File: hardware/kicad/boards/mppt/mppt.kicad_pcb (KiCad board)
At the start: 2 copper layers, 140 x 68 mm, 21 parts, among them J1 PV ind, J2 til lager (V3), J3 sense -> Arduino, Q1 TIP41A, U1 LM358

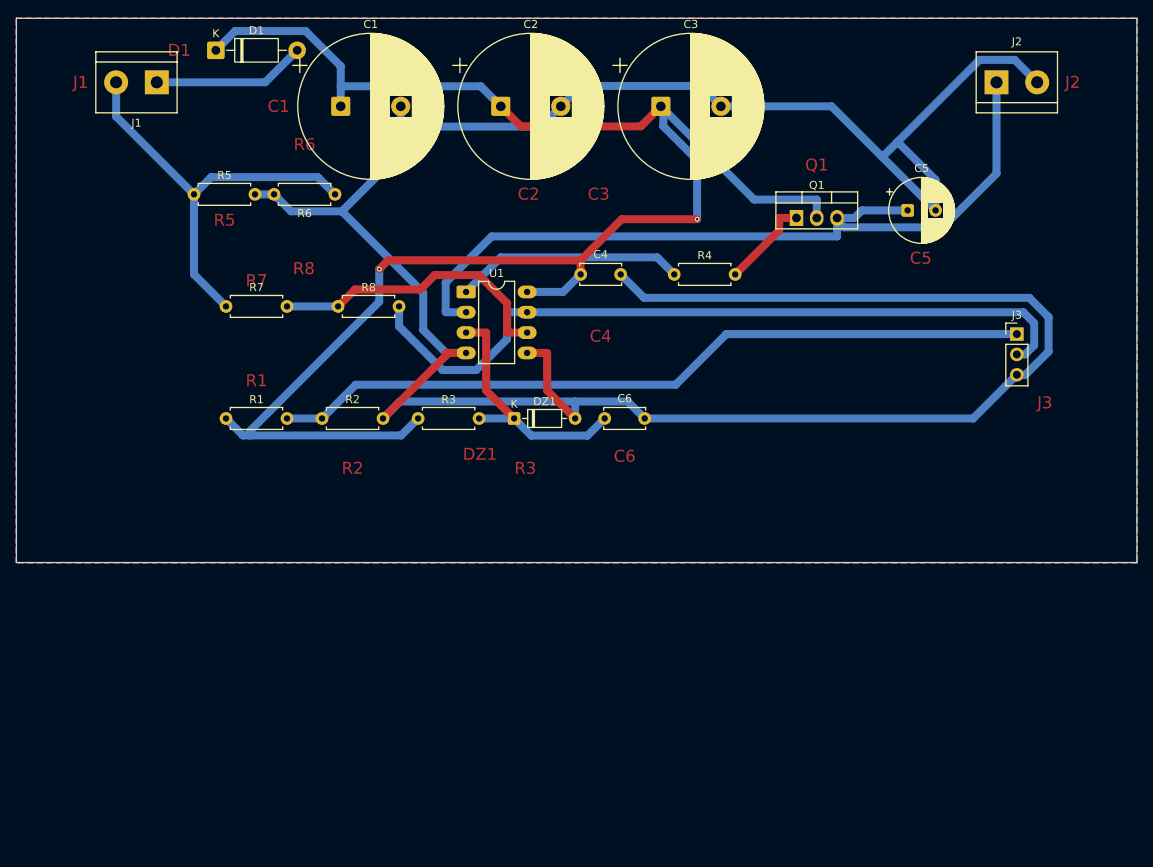
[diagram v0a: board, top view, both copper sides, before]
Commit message: Move all boards to the 104x104 jig format with compact placement
The laser positioning jig takes an exactly 109x109 mm copper blank, so every
board now has identical 104x104 edge cuts (2.5 mm rim). pcb_build.py:
- fixed JIG_W/JIG_H outline, hard failure if content overflows the square
- compact packing: 5 mm bbox gaps (was 8), squarish component cluster below
  the connector zone instead of full-width rows
- mppt/current_sense PLACE layouts re-arranged for the square and tightened

All 7 boards rerouted: 0 unconnected, 0 real DRC errors, and no vias needed
anywhere (the square format routes better than the old elongated boards).
Production DXF/gerbers re-exported; README run-plan updated for the jig
(cut blanks to exactly 109x109, all boards share the same size now).
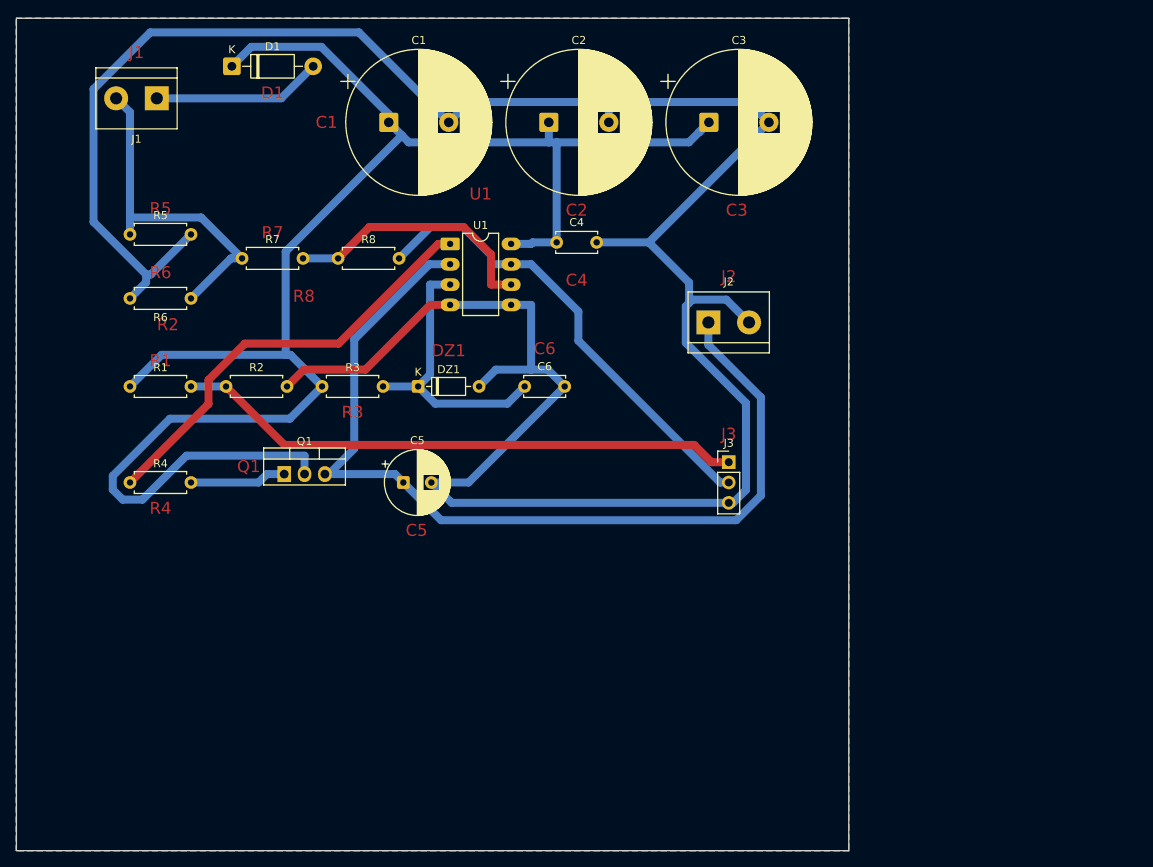
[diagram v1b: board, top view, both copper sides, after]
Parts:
- moved R4 72.8 mm to (34.2, 78.0)
- moved C5 71.6 mm to (68.3, 78.0)
- moved Q1 71.6 mm to (53.5, 77.0)
- moved J2 46.9 mm to (106.5, 58.0)
- moved J3 39.4 mm to (109.0, 75.5)
- moved R6 22.2 mm to (41.8, 55.0)
- moved DZ1 12.6 mm to (70.2, 66.0)
- moved R1 12.6 mm to (34.2, 66.0)
- moved R2 12.6 mm to (46.2, 66.0)
- moved R3 12.6 mm to (58.2, 66.0)
- moved C6 10.8 mm to (83.5, 66.0)
- moved R5 9.43 mm to (34.2, 47.0)
- moved C1 6.32 mm to (66.5, 33.0)
- moved C2 6.32 mm to (86.5, 33.0)
- moved C3 6.32 mm to (106.5, 33.0)
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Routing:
- net /PV_I: track 95.0 -> 58.8 mm
- net /U1A_OUT: track 28.7 -> 54.1 mm
- net /PV_V: track 95.6 -> 71.1 mm
- net GND: track 341.5 -> 326.6 mm
- net /V3_OUT: track 103.5 -> 116.5 mm
- net /PV_RET: track 53.1 -> 42.3 mm
- net /PV_BUS: track 216.2 -> 212.0 mm, vias 2 -> 0
- net /U1B_FB: track 36.7 -> 32.8 mm
- net /VREF: track 32.1 -> 35.3 mm
- net /PV_PLUS: track 19.2 -> 21.2 mm
- net /Q1_B: track 11.5 -> 12.1 mm
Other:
- board size 140 x 68 mm -> 104 x 104 mm
- board text added: "R4"
- board text added: "U1"

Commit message: Condense and center all boards in the jig outline; reroute drive_circuit
Placement (pcb_build.py): connector columns now hug the component block
instead of sitting at the board edges, and the whole cluster is translated to
the center of the 104x104 outline - nothing sits next to the edge cuts
anymore. Fail-hard check if a cluster outgrows the jig.

drive_circuit keeps the hand-made GUI placement but is rerouted with the
two-stage flow: 43 top tracks + 1 via from the GUI autoroute down to 20
pin-to-pin bridges, no via. New tools/strip_routing.py removes existing
routing textually (sexpdata) - in-process pcbnew Remove() access-violates.

All 7 boards: 0 unconnected, 0 real DRC errors, no vias anywhere; buck is
now fully single-sided (0 top tracks). Production files re-exported.
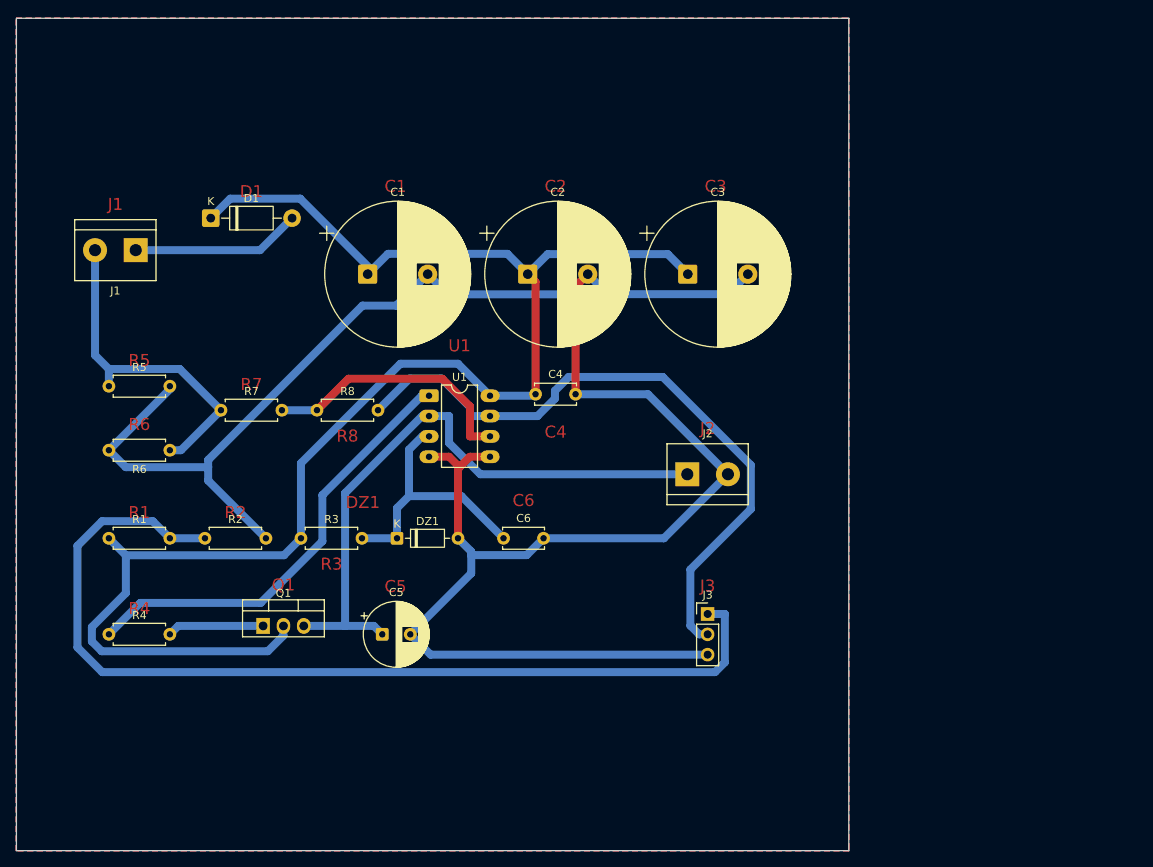
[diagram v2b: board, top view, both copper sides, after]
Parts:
- moved J3 19.2 mm to (106.4, 94.4)
- moved C1 19.2 mm to (63.9, 52.0)
- moved C2 19.2 mm to (83.9, 52.0)
- moved C3 19.2 mm to (103.9, 52.0)
- moved C4 19.2 mm to (84.9, 67.0)
- moved C5 19.2 mm to (65.7, 97.0)
- moved C6 19.2 mm to (80.9, 85.0)
- moved D1 19.2 mm to (44.3, 45.0)
- moved DZ1 19.2 mm to (67.6, 85.0)
- moved J1 19.2 mm to (34.9, 49.0)
- moved J2 19.2 mm to (103.8, 77.0)
- moved Q1 19.2 mm to (50.8, 95.9)
- moved R1 19.2 mm to (31.6, 85.0)
- moved R2 19.2 mm to (43.6, 85.0)
- moved R3 19.2 mm to (55.6, 85.0)
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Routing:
- net GND: track 326.6 -> 267.0 mm
- net /PV_V: track 71.1 -> 121.6 mm
- net /V3_OUT: track 116.5 -> 78.6 mm
- net /PV_I: track 58.8 -> 83.8 mm
- net /PV_BUS: track 212.0 -> 194.7 mm
- net /VREF: track 35.3 -> 33.3 mm
- net /U1A_OUT: track 54.1 -> 55.7 mm
